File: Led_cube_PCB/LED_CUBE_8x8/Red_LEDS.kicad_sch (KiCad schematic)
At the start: 100 parts, among them IC16 74AHCT244PW,118, IC19 74AHCT244PW,118, IC20 74AHCT244PW,118, IC21 74AHCT244PW,118, IC22 74AHCT244PW,118, IC4 74AHCT244PW,118, IC5 74AHCT244PW,118, IC6 74AHCT244PW,118, IC7 SN74HCS238DYYR, J3 Conn_02x16_Odd_Even, J4 Conn_02x16_Odd_Even

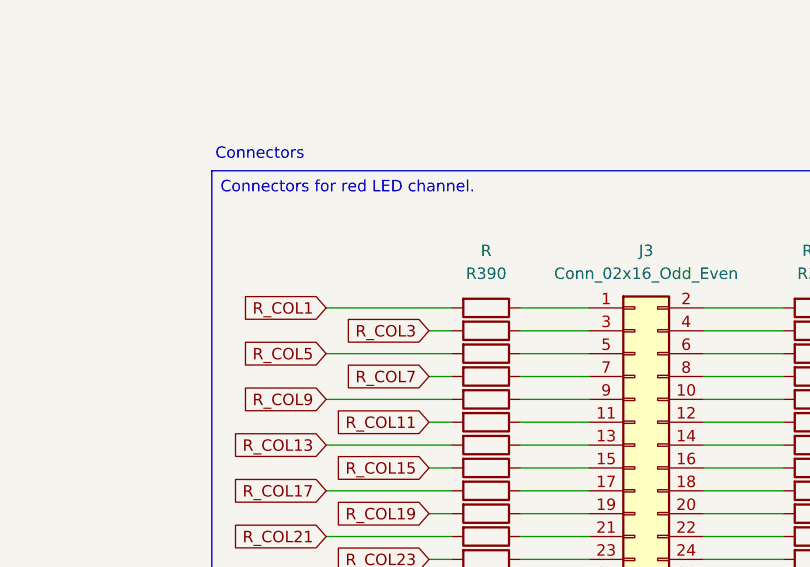
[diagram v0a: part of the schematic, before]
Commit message: Added test points and solder jumpers
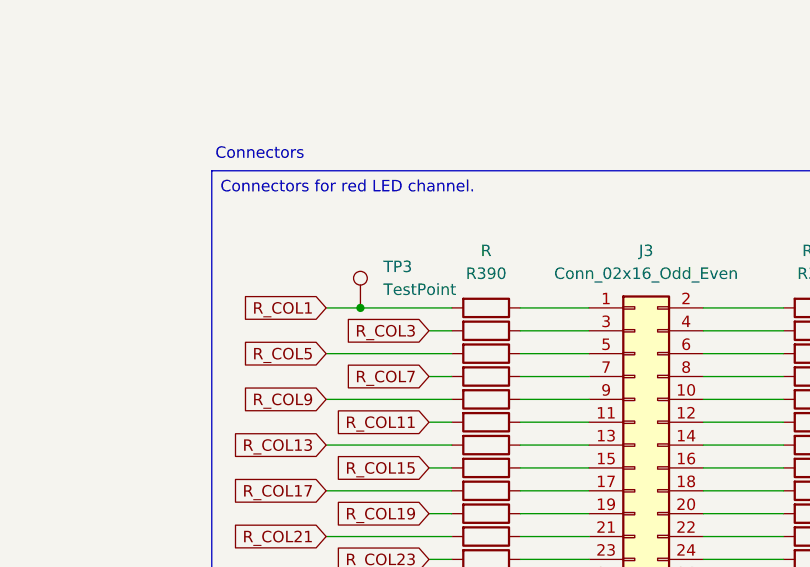
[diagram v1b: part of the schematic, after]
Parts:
- added TP3: TestPoint, TestPoint:TestPoint_Pad_D2.0mm, symbol Connector:TestPoint
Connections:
- net R_COL1: now also TP3.1
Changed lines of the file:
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@@
 	)
 	(junction
+		(at 304.8 92.71)
+		(diameter 0)
+		(color 0 0 0 0)
+	)
+	(junction
 		(at 204.47 88.9)
 		(diameter 0)
@@
 	(wire
 		(pts
-			(xy 300.99 92.71) (xy 314.96 92.71)
+			(xy 300.99 92.71) (xy 304.8 92.71)
 		)
 		(stroke
@@
 	(wire
 		(pts
+			(xy 304.8 92.71) (xy 314.96 92.71)
+		)
+		(stroke
+			(width 0)
+			(type default)
+		)
+	)
+	(wire
+		(pts
 			(xy 322.58 110.49) (xy 330.2 110.49)
 		)
@@
 					(unit 1)
 				)
+			)
+		)
+	)
+	(symbol
+		(lib_id "Connector:TestPoint")
+		(at 304.8 92.71 0)
+		(unit 1)
+		(body_style 1)
+		(exclude_from_sim no)
+		(in_bom yes)
+		(on_board yes)
+		(in_pos_files yes)
+		(dnp no)
+		(fields_autoplaced yes)
+		(property "Reference" "TP3"
+			(at 307.34 88.1379 0)
+			(show_name no)
+			(do_not_autoplace no)
+			(effects
+				(font
+					(size 1.27 1.27)
+				)
+				(justify left)
+			)
+		)
+		(property "Value" "TestPoint"
+			(at 307.34 90.6779 0)
+			(show_name no)
+			(do_not_autoplace no)
+			(effects
+				(font
+					(size 1.27 1.27)
+				)
+				(justify left)
+			)
+		)
+		(property "Footprint" "TestPoint:TestPoint_Pad_D2.0mm"
+			(at 309.88 92.71 0)
+			(hide yes)
+			(show_name no)
+			(do_not_autoplace no)
+			(effects
+				(font
+					(size 1.27 1.27)
+				)
+			)
+		)
+		(property "Datasheet" ""
+			(at 309.88 92.71 0)
+			(hide yes)
+			(show_name no)
+			(do_not_autoplace no)
+			(effects
+				(font
+					(size 1.27 1.27)
+				)
+			)
+		)
+		(property "Description" "test point"
+			(at 304.8 92.71 0)
+			(hide yes)
+			(show_name no)
+			(do_not_autoplace no)
+			(effects
+				(font
+					(size 1.27 1.27)
+				)
+			)
+		)
+		(pin "1"
+		)
+		(instances
+			(project "LED_CUBE_8x8"
+				(path "/b239677e-e361-4439-8200-63fb41f7e03c/39f84ab9-cf03-4ef5-a6b6-c3023701b456"
+					(reference "TP3")
+					(unit 1)
+				)
